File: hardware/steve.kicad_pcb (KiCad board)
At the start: 4 copper layers, 60 x 60 mm, 86 parts, among them Q1 Q_NMOS_GSD, Q2 Q_NMOS_GSD, Q3 Q_NMOS_GSD, Q4 Q_NMOS_GSD, Q5 Q_NMOS_GSD, Q6 Q_NMOS_GSD

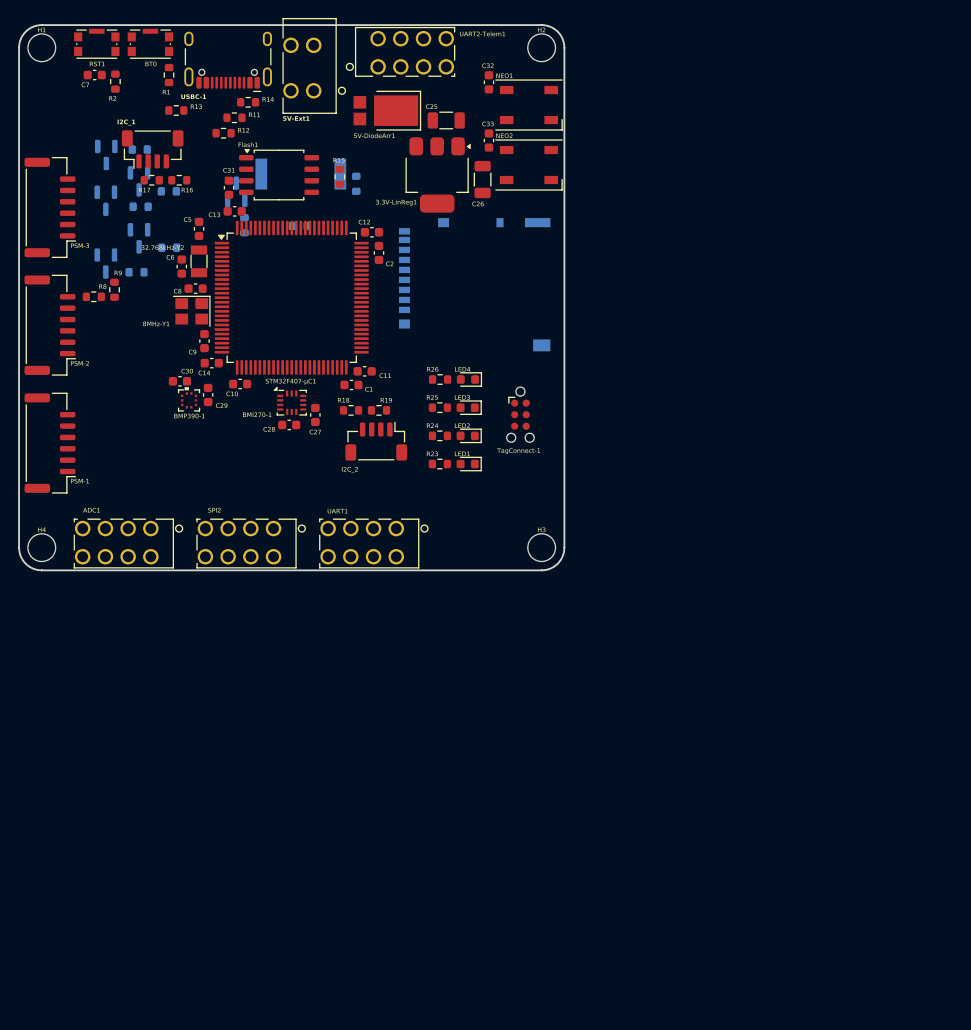
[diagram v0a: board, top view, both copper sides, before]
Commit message: use 50x50mm board
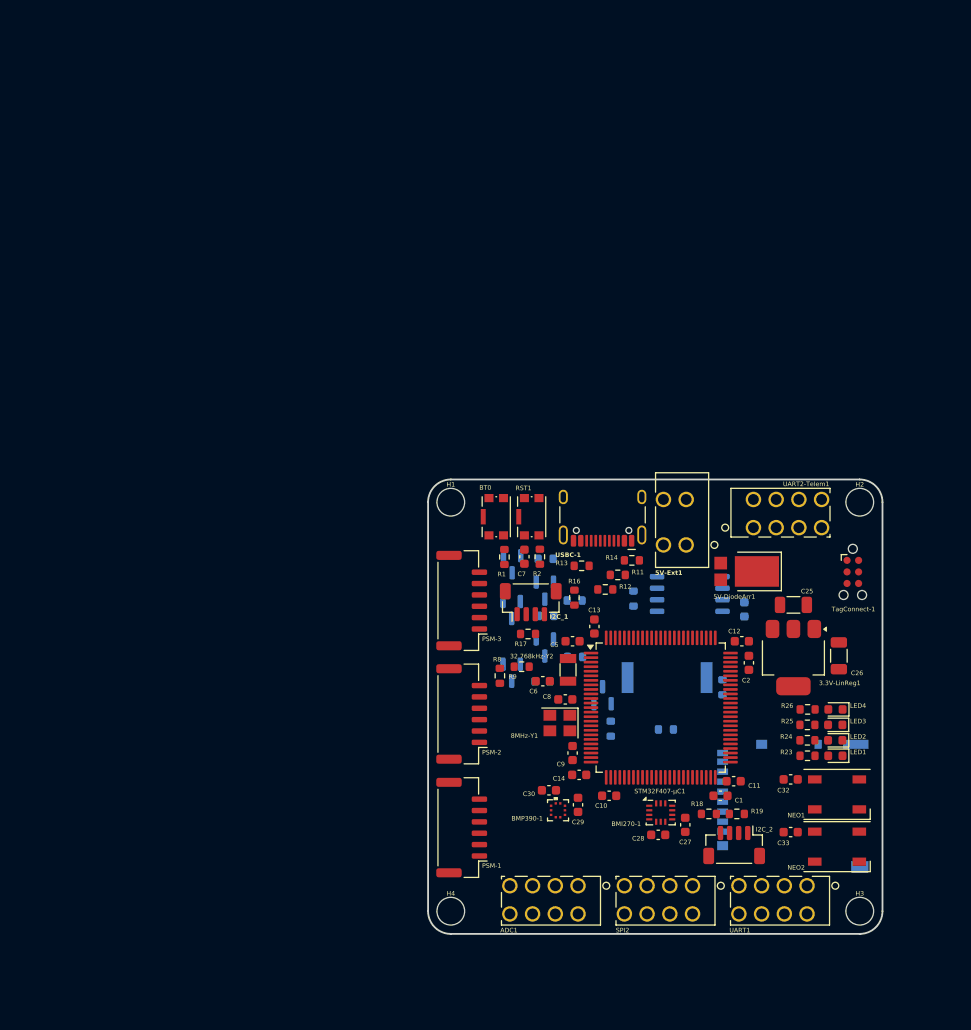
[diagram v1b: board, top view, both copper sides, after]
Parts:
- C31, Flash1, R15: moved to B.Cu
- moved C32 83.6 mm to (139.9, 133.0), turned to 180 degrees
- moved NEO1 83.1 mm to (145.0, 134.7)
- moved C33 83.0 mm to (139.9, 138.8), turned to 180 degrees
- moved NEO2 82.3 mm to (145.0, 140.4)
- moved C31 73.3 mm to (134.8, 114.3)
- moved C7 71.0 mm to (110.6, 108.5), turned to -90 degrees
- moved RST1 70.7 mm to (111.4, 104.1), turned to 90 degrees
- moved R2 70.1 mm to (112.3, 108.5)
- moved R20 68.5 mm to (126.2, 127.5)
- moved R21 68.5 mm to (132.4, 122.9)
- moved Buzzer1 68.5 mm to (126.3, 121.8)
- moved Q1 68.5 mm to (119.2, 123.7)
- moved R22 68.5 mm to (120.1, 127.4)
- moved H1 67.3 mm to (102.5, 102.5)
- moved µSD1 67.2 mm to (140.1, 136.0)
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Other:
- board size 60 x 60 mm -> 50 x 50 mm

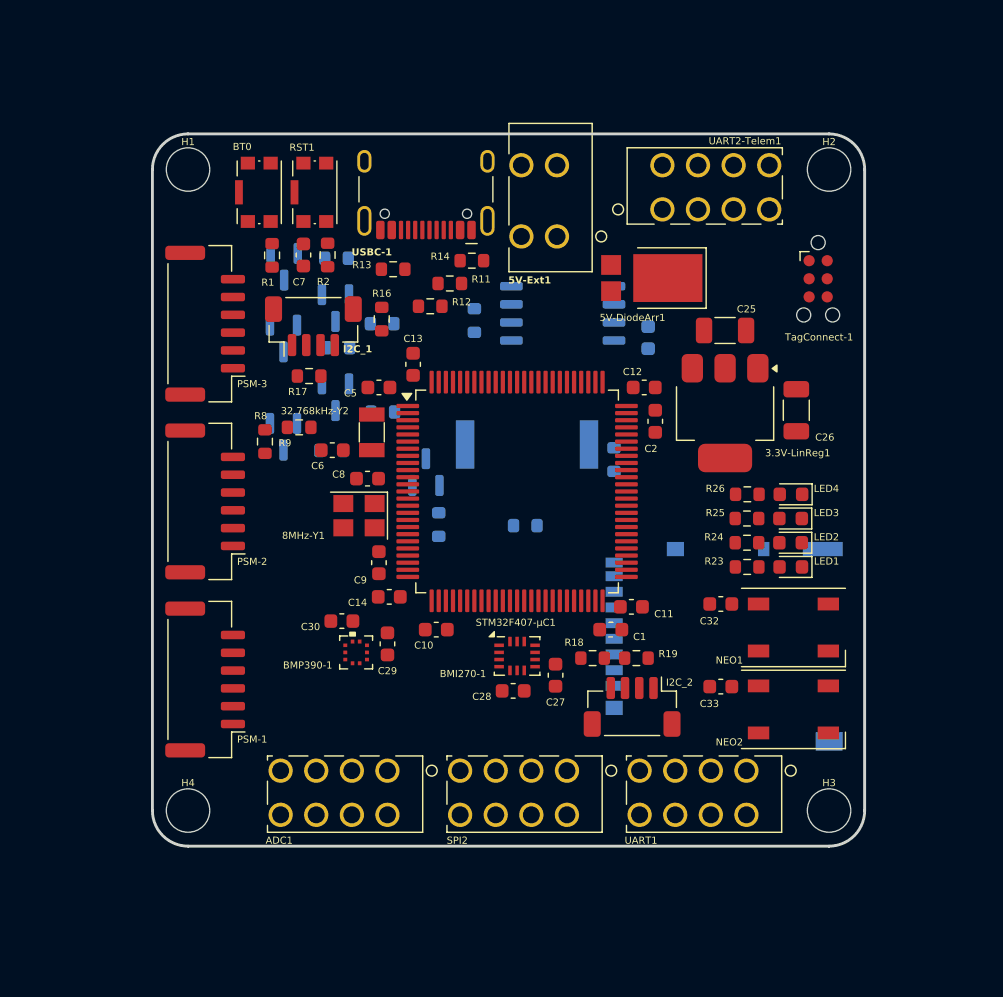
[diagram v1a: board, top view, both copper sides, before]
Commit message: started routing the PCB
started routing the PCB - some components moved a bit. Added GND fill/pour on top and bottom planes, adding extra GND trace width where needed. Also routed short power traces on the top layer. The USB-C 5V trace is a bit long and might need to be moved to layer 2 at some point, but that would require a 70mil trace instead of a 14mil trace for handling 1.5A on an inner layer that is thinner.
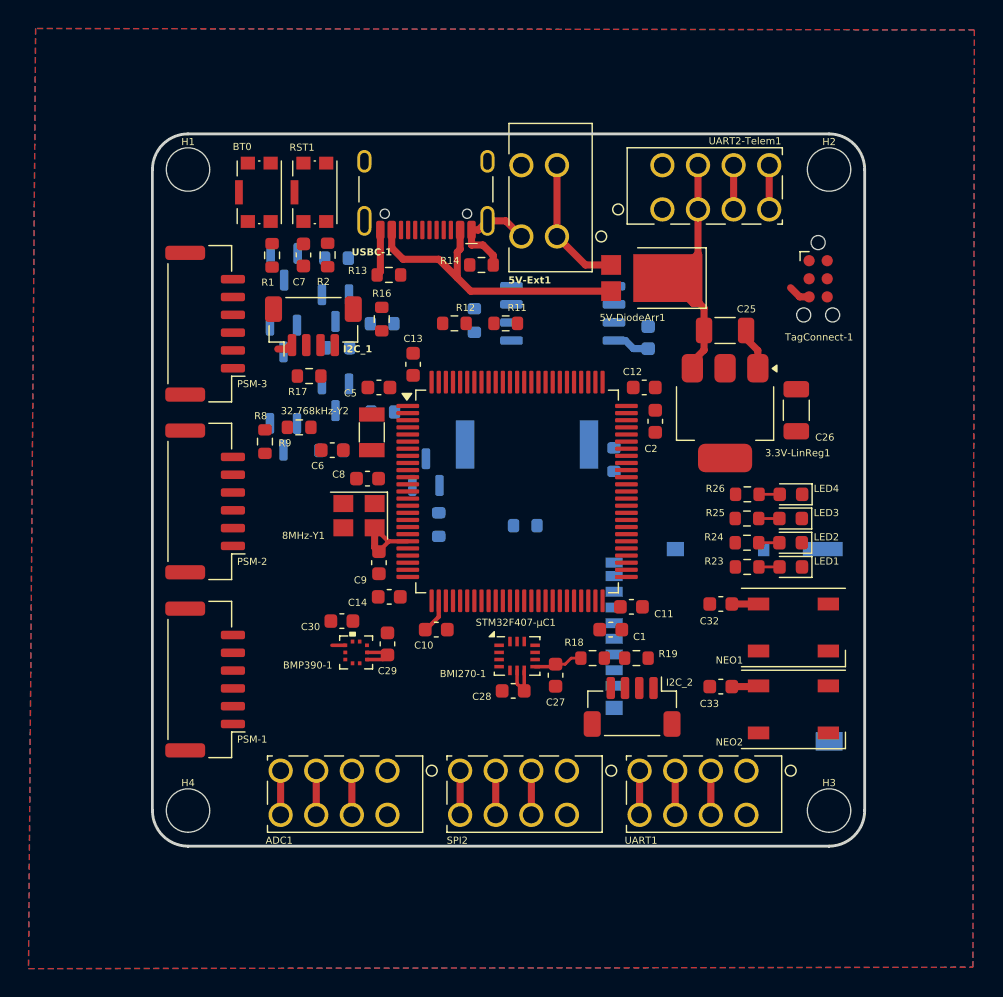
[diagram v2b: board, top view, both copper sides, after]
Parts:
- moved R11 4.82 mm to (124.8, 113.3)
- moved R12 2.08 mm to (121.2, 113.3)
- moved R14 0.74 mm to (123.1, 109.2)
- moved R13 0.50 mm to (116.6, 109.9)
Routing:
- net GND: track 0.00 -> 34.5 mm
- net +5V_USB: track 0.00 -> 21.4 mm
- net +5V: track 0.00 -> 20.8 mm
- net +3.3V: track 0.00 -> 9.66 mm
- net +5V_BATT: track 0.00 -> 9.63 mm
- net UART1_TX_PWM_A9: track 0.00 -> 3.10 mm
- net UART1_RX_PWM_A10: track 0.00 -> 3.10 mm
- net PC3_SPI2_MOSI: track 0.00 -> 3.10 mm
- net PC2_SPI2_MISO: track 0.00 -> 3.10 mm
- net PB13_SPI2_SCK: track 0.00 -> 3.10 mm
- net ADC_C1: track 0.00 -> 3.10 mm
- net ADC_C0: track 0.00 -> 3.10 mm
- net UART2_TX: track 0.00 -> 3.10 mm
- net UART2_RX: track 0.00 -> 3.10 mm
- net Net-(LED1-A): track 0.00 -> 1.45 mm
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- added copper zone on B.Cu, net GND
- added copper zone on F.Cu, net GND

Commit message: added first length matched SPI sets
added first length matched SPI sets for the Flash chip and the BMI270. Still need to finish routing the BMI270 and other footprints that use SPI
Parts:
- moved R15 6.77 mm to (129.2, 111.6), turned to 90 degrees
- moved C31 5.61 mm to (129.2, 114.7)
- moved Flash1 5.35 mm to (123.5, 113.3)
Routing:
- net FLASH_CS: track 0.00 -> 8.97 mm, vias 0 -> 2
- net FLASH_SDO: track 0.00 -> 7.37 mm, vias 0 -> 2
- net FLASH_SDI: track 0.00 -> 7.37 mm, vias 0 -> 2
- net FLASH_SCK: track 0.00 -> 7.36 mm, vias 0 -> 2
- net PA6_SPI1_MISO: track 0.00 -> 6.40 mm, vias 0 -> 2
- net PA5_SPI1_SCK: track 0.00 -> 6.39 mm, vias 0 -> 2
- net PA7_SPI1_MOSI: track 0.00 -> 6.39 mm, vias 0 -> 2
- net +3.3V: track 9.66 -> 13.4 mm
- net +5V_USB: track 21.4 -> 22.0 mm, vias 0 -> 3

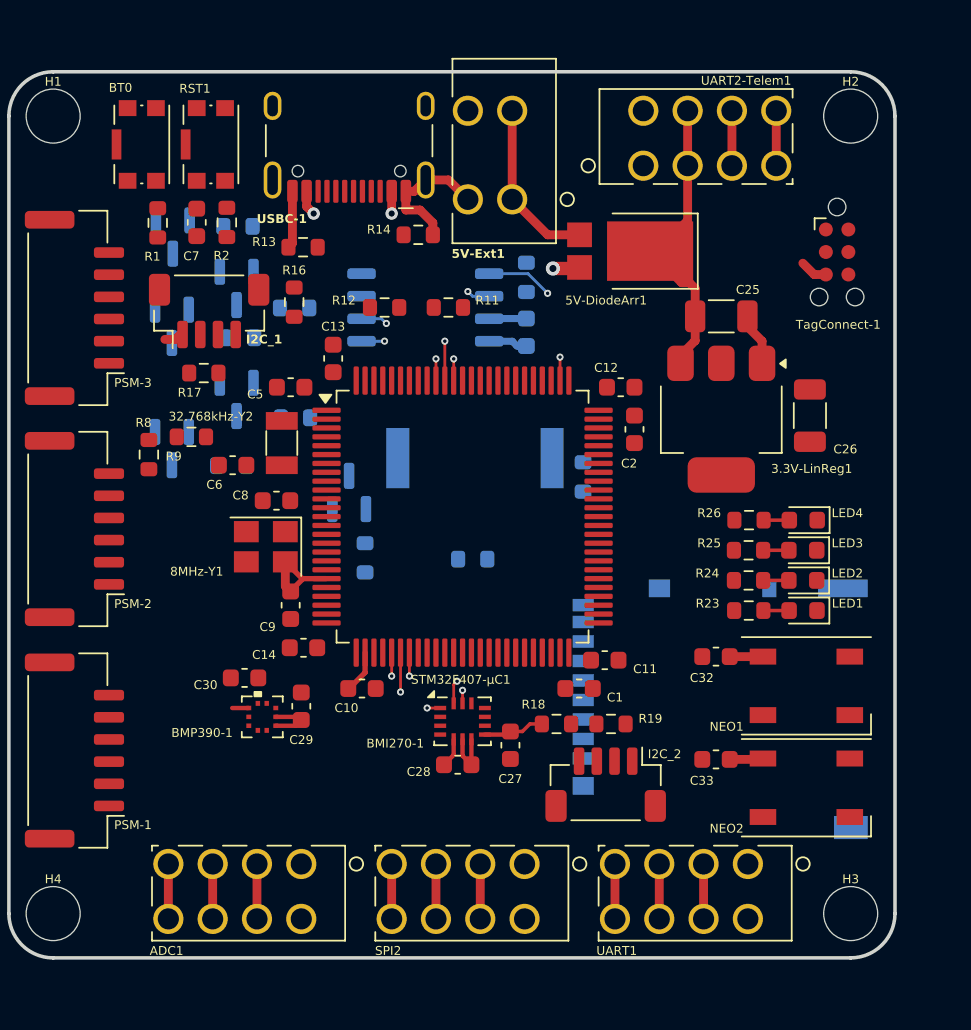
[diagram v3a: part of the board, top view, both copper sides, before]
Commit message: Finished routing traces
Finished routing traces. Also added extra ground vias to stitch the ground planes together. Lessons for next time: power pads (on a microcontroller or other) should immediately get a via; passives can go on the back (including decoupling caps if power vias are close); everything should be spaced further; try not to put 2 unrelated components on top of each other; uC signal traces should be fanned out (mostly inwards) and via'd for ease of use
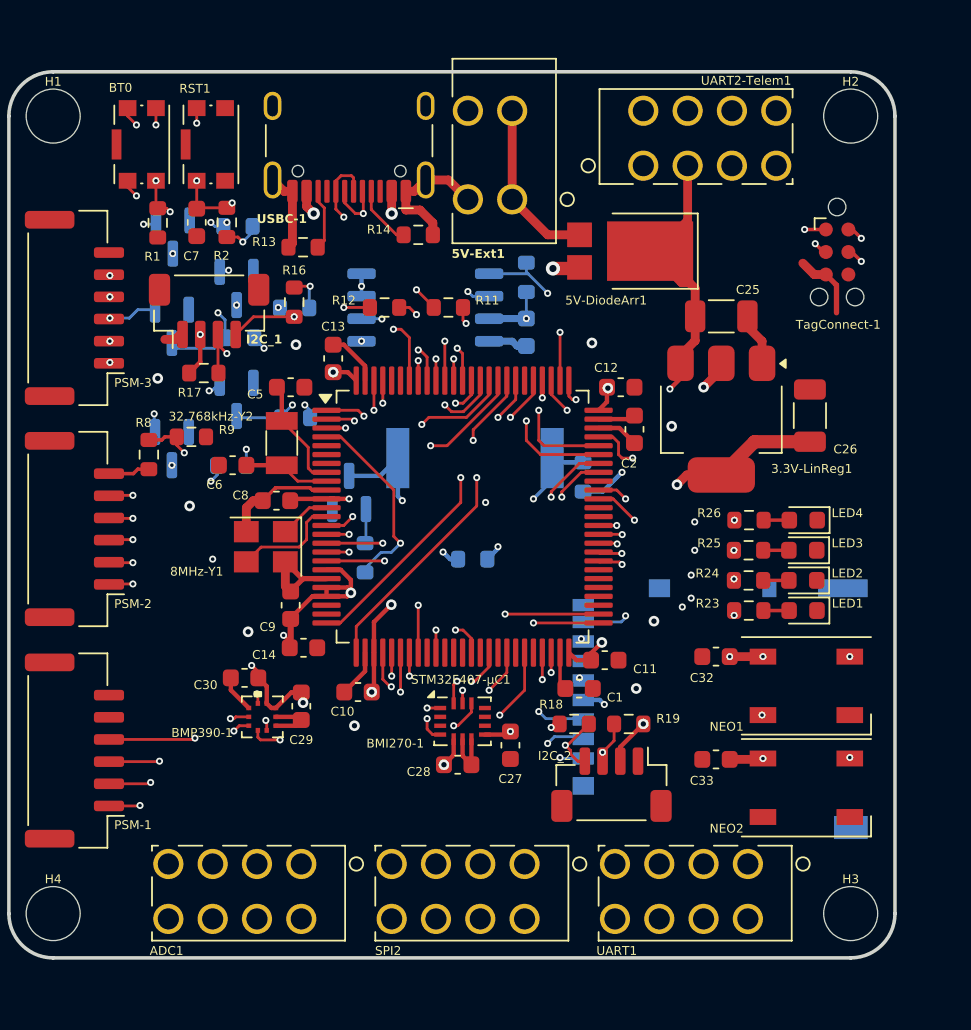
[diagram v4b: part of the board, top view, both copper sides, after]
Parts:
- moved R18 1.00 mm to (131.9, 136.8)
- moved R19 1.00 mm to (135.0, 136.8)
- moved I2C_2 0.32 mm to (134.0, 140.2)
- moved C10 0.30 mm to (119.7, 135.0)
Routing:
- net +3.3V: track 13.4 -> 261.3 mm, vias 0 -> 28
- net ~{RESET}: track 0.00 -> 67.2 mm, vias 0 -> 5
- net PC3_SPI2_MOSI: track 3.10 -> 43.0 mm, vias 0 -> 2
- net PC2_SPI2_MISO: track 3.10 -> 42.9 mm, vias 0 -> 2
- net UART2_TX: track 3.10 -> 42.8 mm, vias 0 -> 1
- net UART2_RX: track 3.10 -> 42.8 mm, vias 0 -> 1
- net PB13_SPI2_SCK: track 3.10 -> 42.5 mm, vias 0 -> 2
- net +5V: track 20.8 -> 51.4 mm, vias 0 -> 5
- net ADC_C1: track 3.10 -> 33.6 mm, vias 0 -> 1
- net SERVO_PWM_4: track 0.00 -> 29.1 mm, vias 0 -> 2
- net CONT1: track 0.00 -> 28.8 mm, vias 0 -> 4
- net SERVO_PWM_3: track 0.00 -> 27.4 mm, vias 0 -> 2
- net SERVO_PWM_1: track 0.00 -> 27.2 mm, vias 0 -> 2
- net SERVO_PWM_2: track 0.00 -> 27.1 mm, vias 0 -> 2
- net ADC_C0: track 3.10 -> 29.4 mm, vias 0 -> 1
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
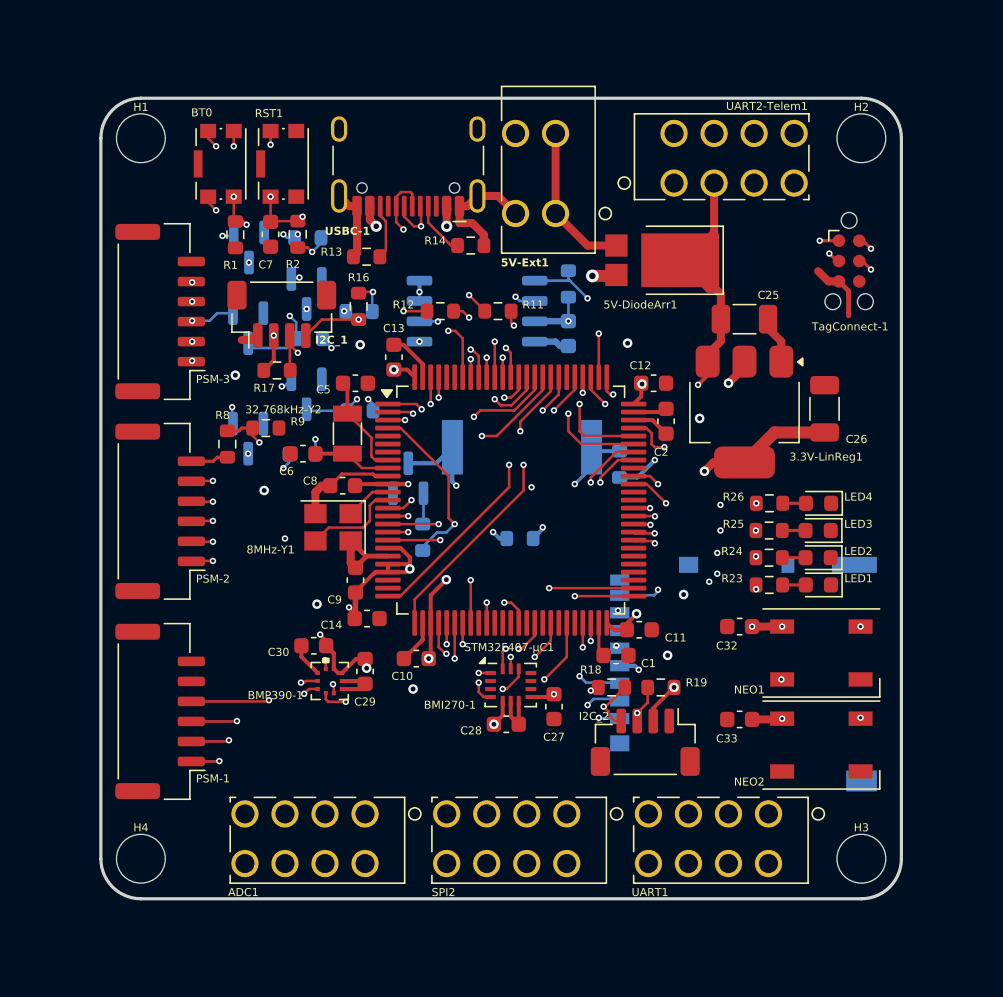
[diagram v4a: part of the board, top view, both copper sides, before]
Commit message: Increase text to 1mm
Increase text length/width to 1mm and line thickness to 0.153mm to match fab capabilities and rules. All capacitor and resistor designators have been hidden to reduce silkscreen clutter.
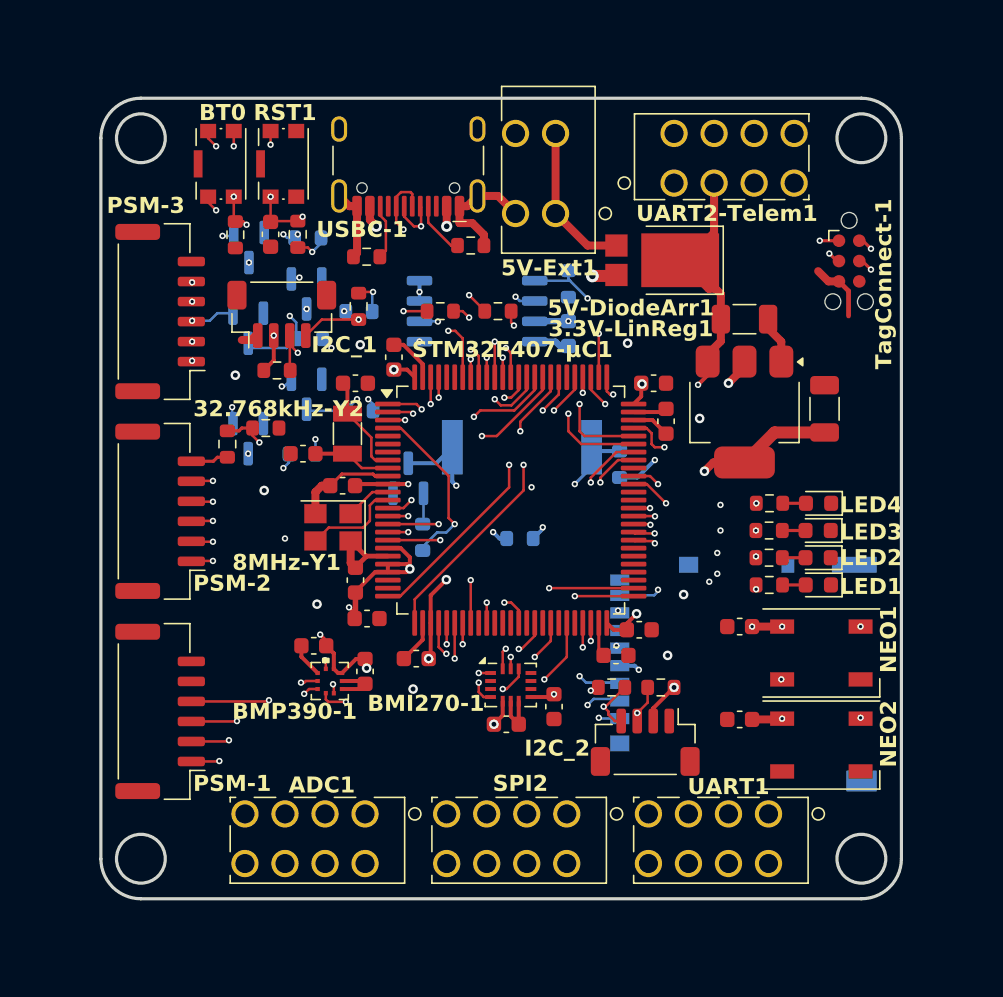
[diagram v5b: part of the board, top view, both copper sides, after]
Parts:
- removed H1, H2, H3, H4: STAND-OFFTIGHT, SparkFun_STM32 Thing Plus:STAND-OFF-TIGHT
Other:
- outline, holes or cut-outs redrawn
